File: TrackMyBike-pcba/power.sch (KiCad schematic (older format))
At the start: 34 parts

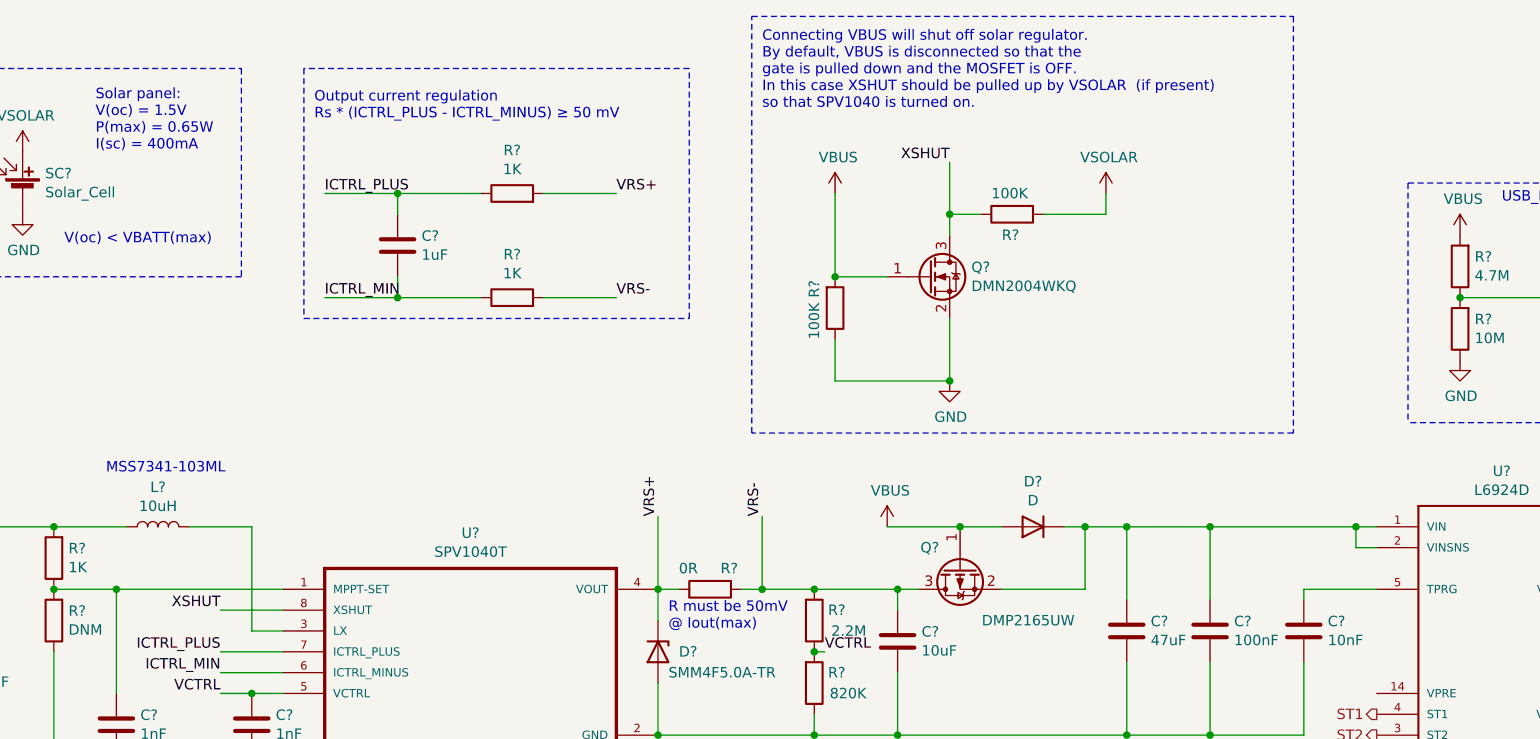
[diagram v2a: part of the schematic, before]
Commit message: Change XSHUT pullup to MPP-SET
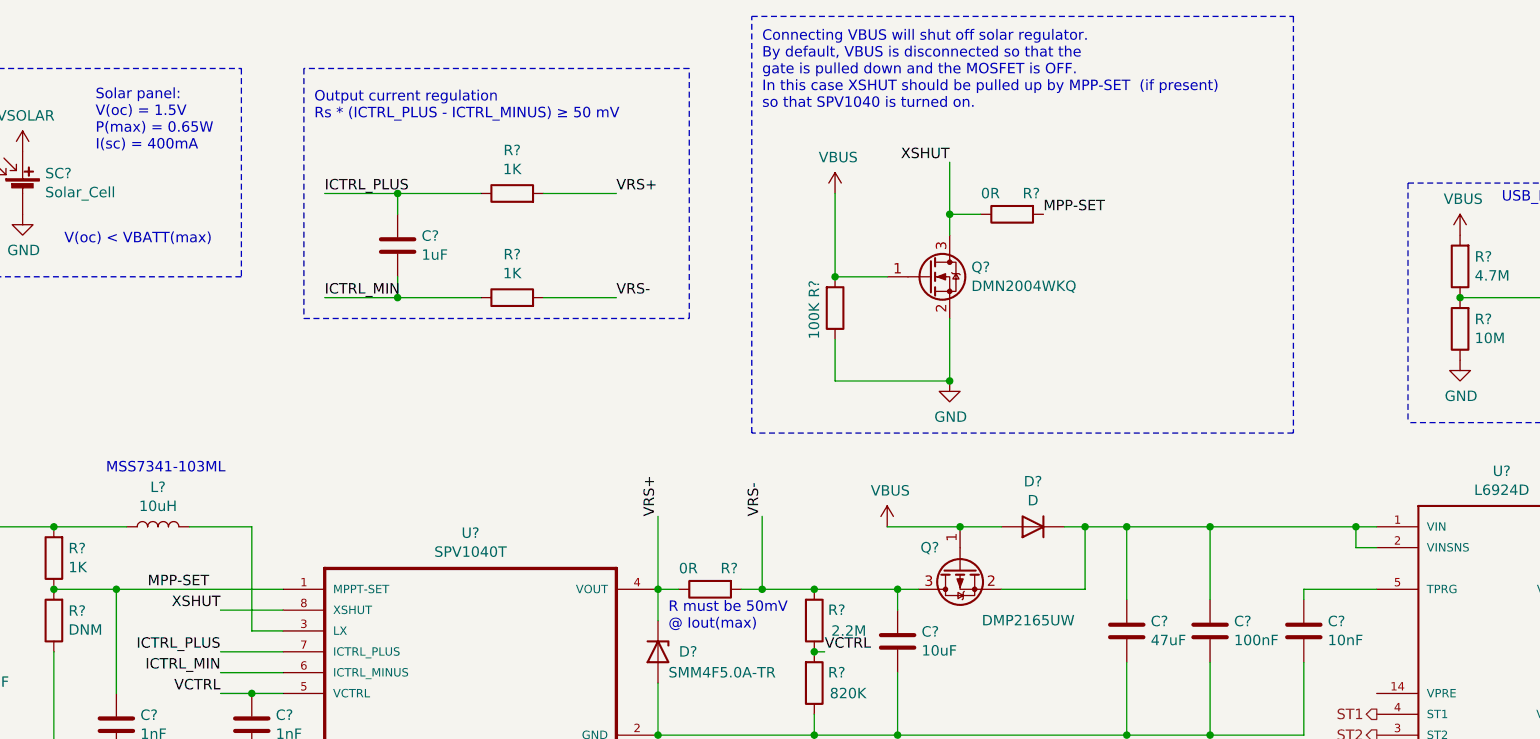
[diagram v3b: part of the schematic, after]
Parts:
- removed R?: 100K, symbol Device:R
- added R?: 0R, symbol Device:R
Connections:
- net XSHUT: now also R?.1
- net MPP-SET: now reaches C?.1, R?.1, R?.2, U?.1 (MPPT-SET)
- net MPP-SET: now also R?.2
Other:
- note added: "Connecting VBUS will shut off solar regulator.\nBy default, VBUS is disconnected so that the \ngate is pulled down and the MOSFET is OFF. \nIn this case XSHUT should be pulled up by MPP-SET (if present) \nso that SPV1040 is turned on."
- note removed: "Connecting VBUS will shut off solar regulator.\nBy default, VBUS is disconnected so that the \ngate is pulled down and the MOSFET is OFF. \nIn this case XSHUT should be pulled up by VSOLAR (if present) \nso that SPV1040 is turned on."
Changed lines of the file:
@@
 	5000 1800 5250 1800
 Text Notes 4650 1000 0    50   ~ 0
-Connecting VBUS will shut off solar regulator.\nBy default, VBUS is disconnected so that the \ngate is pulled down and the MOSFET is OFF. \nIn this case XSHUT should be pulled up by VSOLAR  (if present) \nso that SPV1040 is turned on.
-$Comp
-L Device:R R?
-U 1 1 5F2B803A
-P 5850 1500
-F 0 "R?" V 5950 1550 50  0000 R CNN
-F 1 "100K" V 5750 1600 50  0000 R CNN
-F 2 "" V 5780 1500 50  0001 C CNN
-F 3 "~" H 5850 1500 50  0001 C CNN
-	1    5850 1500
-	0    -1   1    0
-$EndComp
+Connecting VBUS will shut off solar regulator.\nBy default, VBUS is disconnected so that the \ngate is pulled down and the MOSFET is OFF. \nIn this case XSHUT should be pulled up by MPP-SET  (if present) \nso that SPV1040 is turned on.
 Wire Wire Line
 	5000 1400 5000 1800
 Wire Wire Line
 	5550 1250 5550 1500
-$Comp
-L power:VSOLAR #PWR?
-U 1 1 5F2BFF02
-P 6300 1400
-AR Path="/5F2BFF02" Ref="#PWR?"  Part="1"
-AR Path="/5F16A6AE/5F2BFF02" Ref="#PWR?"  Part="1"
-F 0 "#PWR?" H 6300 1250 50  0001 C CNN
-F 1 "VSOLAR" H 6315 1573 50  0000 C CNN
-F 2 "" H 6300 1400 50  0001 C CNN
-F 3 "" H 6300 1400 50  0001 C CNN
-	1    6300 1400
-	1    0    0    -1
-$EndComp
-Wire Wire Line
-	6300 1400 6300 1500
-Wire Wire Line
-	6300 1500 6000 1500
 Wire Wire Line
 	5700 1500 5550 1500
@@
 Text Notes 1300 1650 0    50   ~ 0
 V(oc) < VBATT(max)
+Text Label 1700 3300 0    50   ~ 0
+MPP-SET
+Text Label 6000 1500 0    50   ~ 0
+MPP-SET
+$Comp
+L Device:R R?
+U 1 1 5F2C64B2
+P 5850 1500
+F 0 "R?" V 5750 1450 50  0000 R CNN
+F 1 "0R" V 5750 1650 50  0000 R CNN
+F 2 "" V 5780 1500 50  0001 C CNN
+F 3 "~" H 5850 1500 50  0001 C CNN
+	1    5850 1500
+	0    -1   1    0
+$EndComp
 $EndSCHEMATC

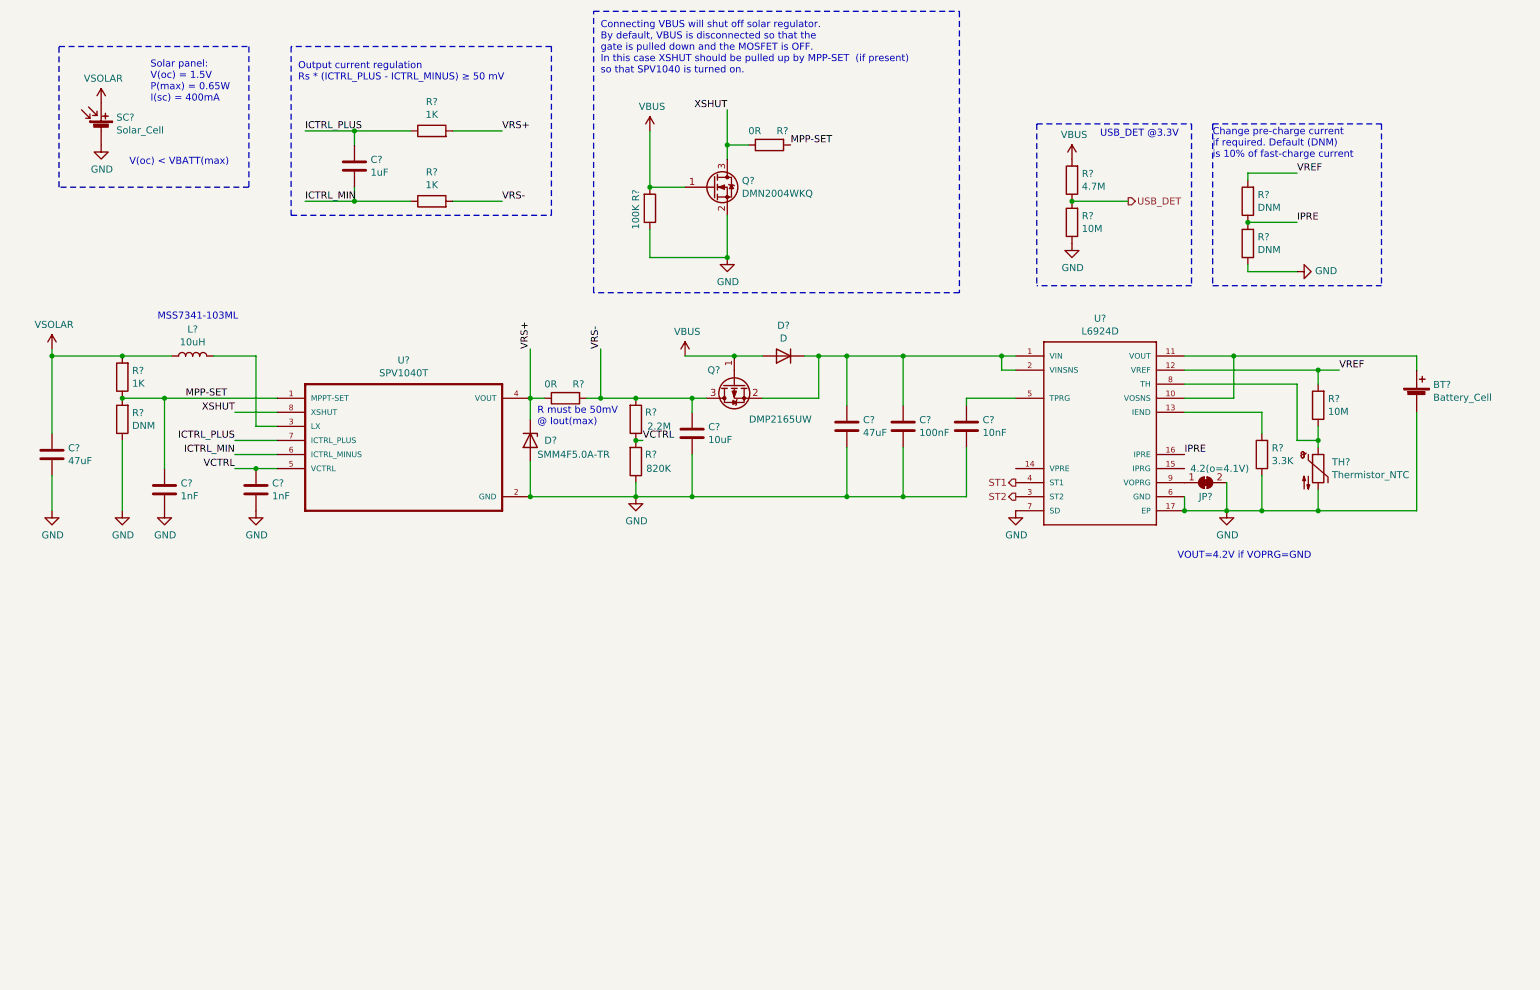
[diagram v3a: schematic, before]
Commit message: Add buck-boost converter to regulate VBAT to 3V3
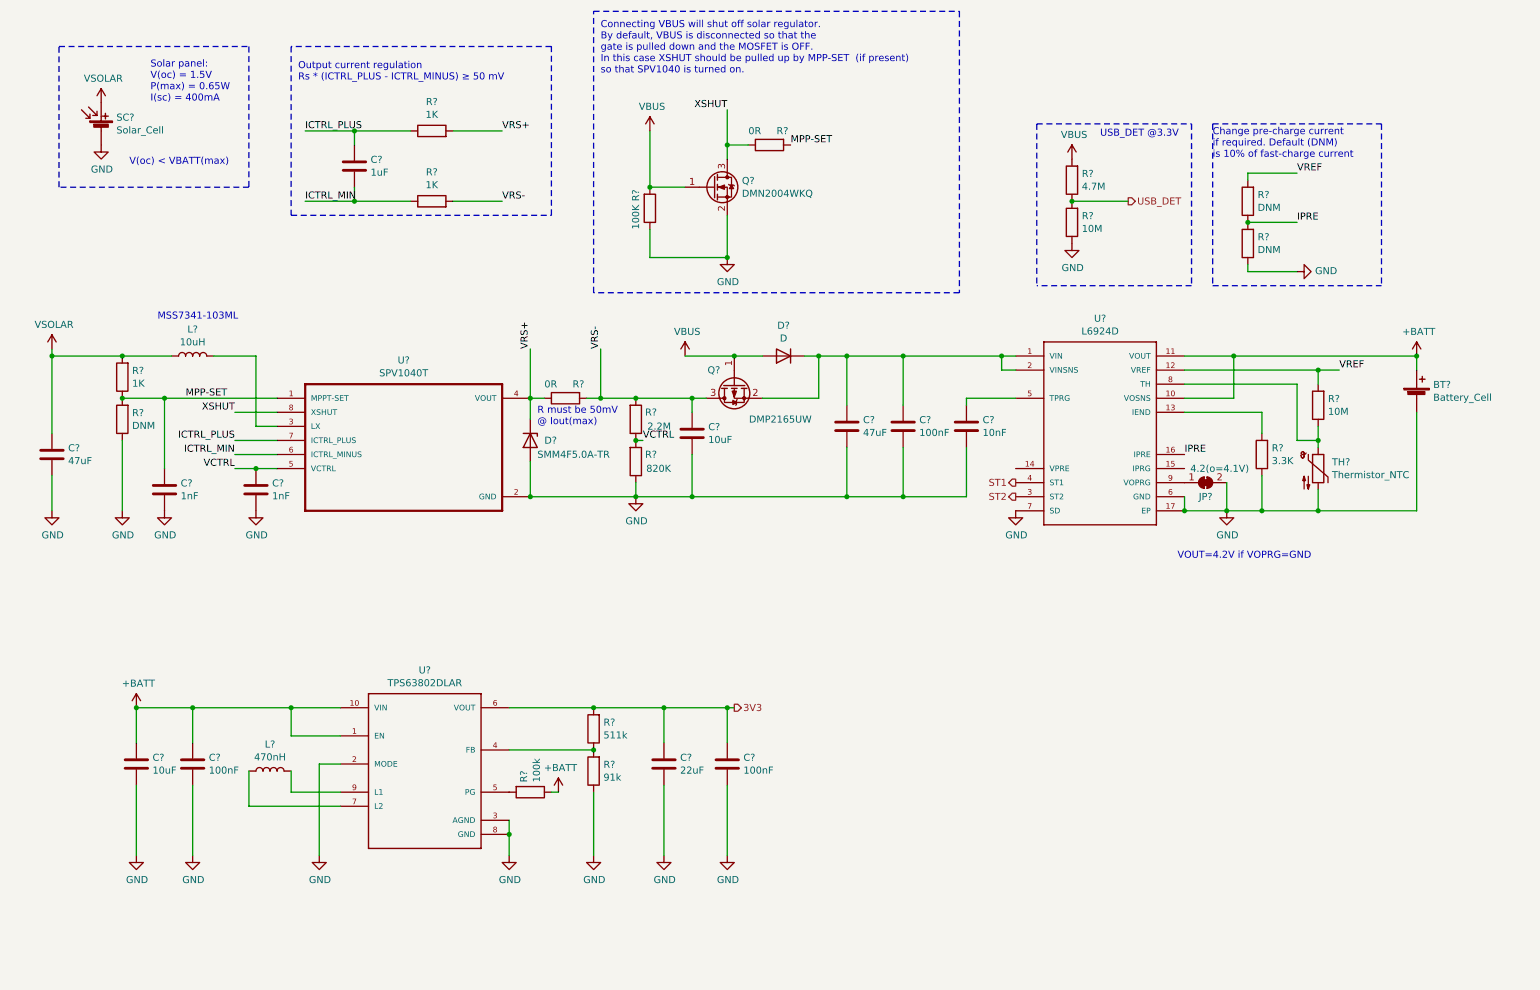
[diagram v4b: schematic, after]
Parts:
- added C?: 22uF, symbol Device:C
- added C?: 10uF, symbol Device:C
- added C? (x2): 100nF, symbol Device:C
- added L?: 470nH, Coilcraft-XFL4015:Coilcraft-XFL4015, symbol Device:L
- added R?: 100k, symbol Device:R
- added R?: 511k, symbol Device:R
- added R?: 91k, symbol Device:R
- added U?: TPS63802DLAR, VREG_TPS63802DLAR, symbol TPS63802DLAR:TPS63802DLAR
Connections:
- net GND: now also C?.2, C?.2, C?.2, C?.2, R?.1, U?.2 (MODE), U?.3 (AGND), U?.8 (GND)
- net +BATT: now reaches BT?.1 (+), U?.10 (VOSNS), U?.11 (VOUT)
- net +BATT: now also C?.1, C?.1, R?.1, U?.1 (EN), U?.10 (VIN)
- new net: R?.1, R?.2, U?.4 (FB)
- new net: R?.2, U?.5 (PG)
- new net: L?.1, U?.7 (L2)
- new net: L?.2, U?.9 (L1)
- new net 3V3: C?.1, C?.1, R?.2, U?.6 (VOUT)

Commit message: Modify power.sch
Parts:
- added C?: 47uF, symbol Device:C
- R?: value 0R -> 50mOhm
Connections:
- net +1V0: now also C?.1
- net GND: now also C?.2
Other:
- note added: "SPV1040 inductor selection"
- moved on the sheet: BT?, C?, D?, JP?, L?, Q?, R?, SC?, TH?, U?

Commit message: Modify power.sch, add testpoints
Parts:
- added C?: DNM, symbol Device:C
- added R?: 12K, symbol Device:R
- added R?: 0R DNM, symbol Device:R
- added R?: DNM, symbol Device:R
- added R?: 100k DNM, symbol Device:R
- added TP? (x10): TestPoint, symbol Connector:TestPoint
- C?: value 10nF -> 30nF
- R?: value 10M -> 620R
- R?: value 50mOhm -> 0.05R
- R?: value 3.3K -> 1K
- R? (x2): value DNM -> 0R DNM
- TH?: value Thermistor_NTC -> 220R; footprint (none) -> Resistor_SMD:R_0805_2012Metric
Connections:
- net labels added: IPRG, SD, VPRE, Vgauge
- wire segments 132 -> 143
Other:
- note added: "Connecting VBUS will shut off solar regulator.\nBy default, VBUS is disconnected so that the \ngate is pulled down and the MOSFET is OFF. \nIn this case XSHUT should be pulled up by \nMPP-SET (if present) \nso that SPV1040 is turned on."
- note added: "Ctprg"
- note added: "NCP21XM221J03RA"
- note added: "Rend"
- note added: "Rntc(0C) \n= Rup \n= 627R"
- note added: "Rprg"
- note added: "Rvpre"
- note removed: "Connecting VBUS will shut off solar regulator.\nBy default, VBUS is disconnected so that the \ngate is pulled down and the MOSFET is OFF. \nIn this case XSHUT should be pulled up by MPP-SET (if present) \nso that SPV1040 is turned on."
- moved on the sheet: C?, R?

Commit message: add footprints to some components
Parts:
- removed R?: 1K, symbol Device:R
- added R?: 1K, Resistor_SMD:R_1206_3216Metric_Pad1.42x1.75mm_HandSolder, symbol Device:R
- BT?, SC?: footprint (none) -> Connector_JST:JST_PH_S2B-PH-SM4-TB_1x02-1MP_P2.00mm_Horizontal
- R? (x21): footprint (none) -> Resistor_SMD:R_1206_3216Metric_Pad1.42x1.75mm_HandSolder
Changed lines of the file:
@@
 F 0 "R?" H 7480 1204 50  0000 R CNN
 F 1 "10M" H 7480 1295 50  0000 R CNN
-F 2 "" V 7480 1250 50  0001 C CNN
+F 2 "Resistor_SMD:R_1206_3216Metric_Pad1.42x1.75mm_HandSolder" V 7480 1250 50  0001 C CNN
 F 3 "~" H 7550 1250 50  0001 C CNN
 	1    7550 1250
@@
 F 0 "R?" H 7480 904 50  0000 R CNN
 F 1 "4.7M" H 7480 995 50  0000 R CNN
-F 2 "" V 7480 950 50  0001 C CNN
+F 2 "Resistor_SMD:R_1206_3216Metric_Pad1.42x1.75mm_HandSolder" V 7480 950 50  0001 C CNN
 F 3 "~" H 7550 950 50  0001 C CNN
 	1    7550 950
@@
 F 0 "R?" H 9780 4254 50  0000 R CNN
 F 1 "620R" H 9780 4345 50  0000 R CNN
-F 2 "" V 9780 4300 50  0001 C CNN
+F 2 "Resistor_SMD:R_1206_3216Metric_Pad1.42x1.75mm_HandSolder" V 9780 4300 50  0001 C CNN
 F 3 "~" H 9850 4300 50  0001 C CNN
 	1    9850 4300
@@
 F 0 "R?" V 3657 1150 50  0000 C CNN
 F 1 "1K" V 3566 1150 50  0000 C CNN
-F 2 "" V 3380 1150 50  0001 C CNN
+F 2 "Resistor_SMD:R_1206_3216Metric_Pad1.42x1.75mm_HandSolder" V 3380 1150 50  0001 C CNN
 F 3 "~" H 3450 1150 50  0001 C CNN
 	1    3450 1150
-	0    -1   -1   0
-$EndComp
-$Comp
-L Device:R R?
-U 1 1 5F203FF2
-P 3450 1650
-F 0 "R?" V 3657 1650 50  0000 C CNN
-F 1 "1K" V 3566 1650 50  0000 C CNN
-F 2 "" V 3380 1650 50  0001 C CNN
-F 3 "~" H 3450 1650 50  0001 C CNN
-	1    3450 1650
 	0    -1   -1   0
 $EndComp
@@
 F 0 "R?" H 5150 4350 50  0000 R CNN
 F 1 "2.2M" H 5250 4450 50  0000 R CNN
-F 2 "" V 4930 4400 50  0001 C CNN
+F 2 "Resistor_SMD:R_1206_3216Metric_Pad1.42x1.75mm_HandSolder" V 4930 4400 50  0001 C CNN
 F 3 "~" H 5000 4400 50  0001 C CNN
 	1    5000 4400
@@
 F 0 "R?" H 5150 4650 50  0000 R CNN
 F 1 "820K" H 5250 4750 50  0000 R CNN
-F 2 "" V 4930 4700 50  0001 C CNN
+F 2 "Resistor_SMD:R_1206_3216Metric_Pad1.42x1.75mm_HandSolder" V 4930 4700 50  0001 C CNN
 F 3 "~" H 5000 4700 50  0001 C CNN
 	1    5000 4700
@@
 F 0 "R?" V 4300 4400 50  0000 R CNN
 F 1 "0.05R" V 4400 4400 50  0000 R CNN
-F 2 "" V 4430 4250 50  0001 C CNN
+F 2 "Resistor_SMD:R_1206_3216Metric_Pad1.42x1.75mm_HandSolder" V 4430 4250 50  0001 C CNN
 F 3 "~" H 4500 4250 50  0001 C CNN
 	1    4500 4250
@@
 F 0 "R?" H 1280 4054 50  0000 R CNN
 F 1 "1K" H 1280 4145 50  0000 R CNN
-F 2 "" V 1280 4100 50  0001 C CNN
+F 2 "Resistor_SMD:R_1206_3216Metric_Pad1.42x1.75mm_HandSolder" V 1280 4100 50  0001 C CNN
 F 3 "~" H 1350 4100 50  0001 C CNN
 	1    1350 4100
@@
 F 0 "R?" H 1280 4354 50  0000 R CNN
 F 1 "DNM" H 1280 4445 50  0000 R CNN
-F 2 "" V 1280 4400 50  0001 C CNN
+F 2 "Resistor_SMD:R_1206_3216Metric_Pad1.42x1.75mm_HandSolder" V 1280 4400 50  0001 C CNN
 F 3 "~" H 1350 4400 50  0001 C CNN
 	1    1350 4400
@@
 F 0 "R?" V 4900 1900 50  0000 R CNN
 F 1 "100K" V 4900 2100 50  0000 R CNN
-F 2 "" V 4930 1950 50  0001 C CNN
+F 2 "Resistor_SMD:R_1206_3216Metric_Pad1.42x1.75mm_HandSolder" V 4930 1950 50  0001 C CNN
 F 3 "~" H 5000 1950 50  0001 C CNN
 	1    5000 1950
@@
 F 0 "BT?" H 10668 4346 50  0000 L CNN
 F 1 "Battery_Cell" H 10668 4255 50  0000 L CNN
-F 2 "" V 10550 4310 50  0001 C CNN
+F 2 "Connector_JST:JST_PH_S2B-PH-SM4-TB_1x02-1MP_P2.00mm_Horizontal" V 10550 4310 50  0001 C CNN
 F 3 "~" V 10550 4310 50  0001 C CNN
 	1    10550 4250
@@
 F 0 "R?" H 9380 4604 50  0000 R CNN
 F 1 "1K" H 9380 4695 50  0000 R CNN
-F 2 "" V 9380 4650 50  0001 C CNN
+F 2 "Resistor_SMD:R_1206_3216Metric_Pad1.42x1.75mm_HandSolder" V 9380 4650 50  0001 C CNN
 F 3 "~" H 9450 4650 50  0001 C CNN
 	1    9450 4650
@@
 F 0 "R?" H 8680 1054 50  0000 R CNN
 F 1 "0R DNM" H 8680 1145 50  0000 R CNN
-F 2 "" V 8680 1100 50  0001 C CNN
+F 2 "Resistor_SMD:R_1206_3216Metric_Pad1.42x1.75mm_HandSolder" V 8680 1100 50  0001 C CNN
 F 3 "~" H 8750 1100 50  0001 C CNN
 	1    8750 1100
@@
 F 0 "R?" H 8680 1354 50  0000 R CNN
 F 1 "0R DNM" H 8680 1445 50  0000 R CNN
-F 2 "" V 8680 1400 50  0001 C CNN
+F 2 "Resistor_SMD:R_1206_3216Metric_Pad1.42x1.75mm_HandSolder" V 8680 1400 50  0001 C CNN
 F 3 "~" H 8750 1400 50  0001 C CNN
 	1    8750 1400
@@
 F 0 "SC?" H 1208 1246 50  0000 L CNN
 F 1 "Solar_Cell" H 1208 1155 50  0000 L CNN
-F 2 "" V 1100 1210 50  0001 C CNN
+F 2 "Connector_JST:JST_PH_S2B-PH-SM4-TB_1x02-1MP_P2.00mm_Horizontal" V 1100 1210 50  0001 C CNN
 F 3 "~" V 1100 1210 50  0001 C CNN
 	1    1100 1150
@@
 F 0 "R?" V 5750 1450 50  0000 R CNN
 F 1 "0R" V 5750 1650 50  0000 R CNN
-F 2 "" V 5780 1500 50  0001 C CNN
+F 2 "Resistor_SMD:R_1206_3216Metric_Pad1.42x1.75mm_HandSolder" V 5780 1500 50  0001 C CNN
 F 3 "~" H 5850 1500 50  0001 C CNN
 	1    5850 1500
@@
 F 0 "R?" H 3680 6704 50  0000 R CNN
 F 1 "100k" H 3680 6795 50  0000 R CNN
-F 2 "" V 3680 6750 50  0001 C CNN
+F 2 "Resistor_SMD:R_1206_3216Metric_Pad1.42x1.75mm_HandSolder" V 3680 6750 50  0001 C CNN
 F 3 "~" H 3750 6750 50  0001 C CNN
 	1    3750 6750
@@
 F 0 "R?" H 4130 6254 50  0000 R CNN
 F 1 "511k" H 4130 6345 50  0000 R CNN
-F 2 "" V 4130 6300 50  0001 C CNN
+F 2 "Resistor_SMD:R_1206_3216Metric_Pad1.42x1.75mm_HandSolder" V 4130 6300 50  0001 C CNN
 F 3 "~" H 4200 6300 50  0001 C CNN
 	1    4200 6300
@@
 F 0 "R?" H 4130 6554 50  0000 R CNN
 F 1 "91k" H 4130 6645 50  0000 R CNN
-F 2 "" V 4130 6600 50  0001 C CNN
+F 2 "Resistor_SMD:R_1206_3216Metric_Pad1.42x1.75mm_HandSolder" V 4130 6600 50  0001 C CNN
 F 3 "~" H 4200 6600 50  0001 C CNN
 	1    4200 6600
@@
 F 0 "R?" H 7380 2054 50  0000 R CNN
 F 1 "12K" H 7380 2145 50  0000 R CNN
-F 2 "" V 7380 2100 50  0001 C CNN
+F 2 "Resistor_SMD:R_1206_3216Metric_Pad1.42x1.75mm_HandSolder" V 7380 2100 50  0001 C CNN
 F 3 "~" H 7450 2100 50  0001 C CNN
 	1    7450 2100
@@
 F 0 "R?" V 5750 3500 50  0000 R CNN
 F 1 "0R DNM" V 5650 3700 50  0000 R CNN
-F 2 "" V 5780 3500 50  0001 C CNN
+F 2 "Resistor_SMD:R_1206_3216Metric_Pad1.42x1.75mm_HandSolder" V 5780 3500 50  0001 C CNN
 F 3 "~" H 5850 3500 50  0001 C CNN
 	1    5850 3500
@@
 F 0 "R?" H 7880 2054 50  0000 R CNN
 F 1 "DNM" H 7880 2145 50  0000 R CNN
-F 2 "" V 7880 2100 50  0001 C CNN
+F 2 "Resistor_SMD:R_1206_3216Metric_Pad1.42x1.75mm_HandSolder" V 7880 2100 50  0001 C CNN
 F 3 "~" H 7950 2100 50  0001 C CNN
 	1    7950 2100
@@
 F 0 "R?" H 7850 5250 50  0000 R CNN
 F 1 "100k DNM" H 8150 5350 50  0000 R CNN
-F 2 "" V 7630 5300 50  0001 C CNN
+F 2 "Resistor_SMD:R_1206_3216Metric_Pad1.42x1.75mm_HandSolder" V 7630 5300 50  0001 C CNN
 F 3 "~" H 7700 5300 50  0001 C CNN
 	1    7700 5300
@@
 	1    0    0    -1
 $EndComp
+$Comp
+L Device:R R?
+U 1 1 5F4C2270
+P 3450 1650
+F 0 "R?" V 3657 1650 50  0000 C CNN
+F 1 "1K" V 3566 1650 50  0000 C CNN
+F 2 "Resistor_SMD:R_1206_3216Metric_Pad1.42x1.75mm_HandSolder" V 3380 1650 50  0001 C CNN
+F 3 "~" H 3450 1650 50  0001 C CNN
+	1    3450 1650
+	0    -1   -1   0
+$EndComp
 $EndSCHEMATC
